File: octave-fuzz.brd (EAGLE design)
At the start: 77.1 x 81.3 mm, 56 parts, among them T1 2N5089, T2 2N5089, T3 2N5089, T4 2N5089, T5 2N5089

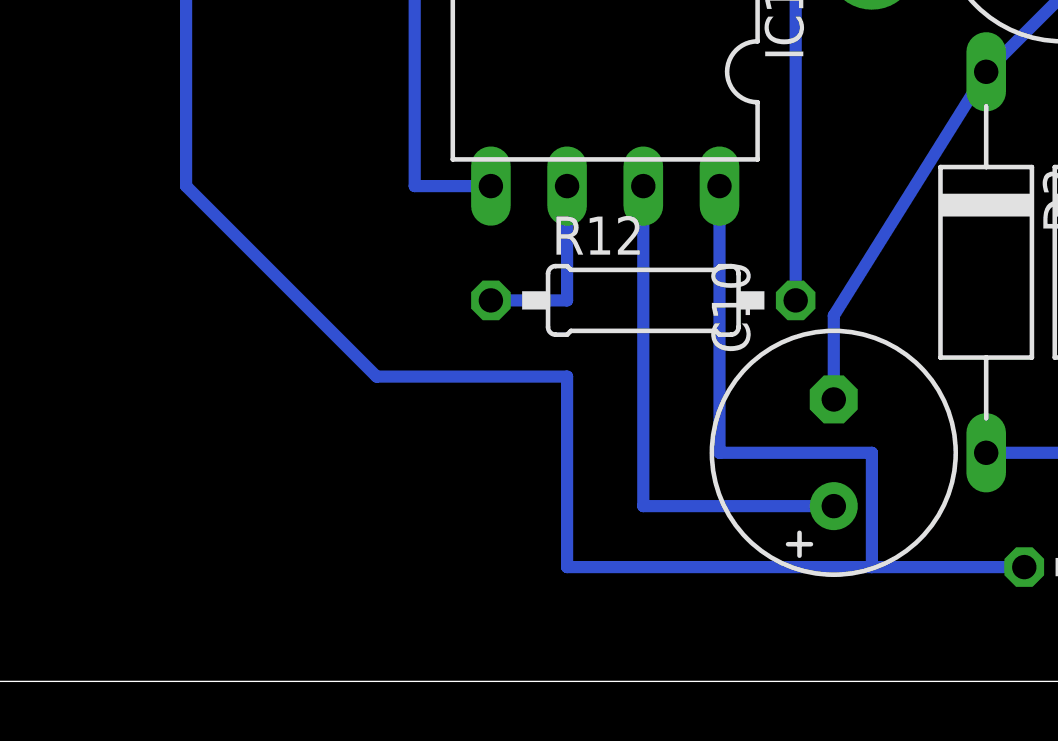
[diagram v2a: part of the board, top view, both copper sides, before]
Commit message: added a missing resistor and edited component values
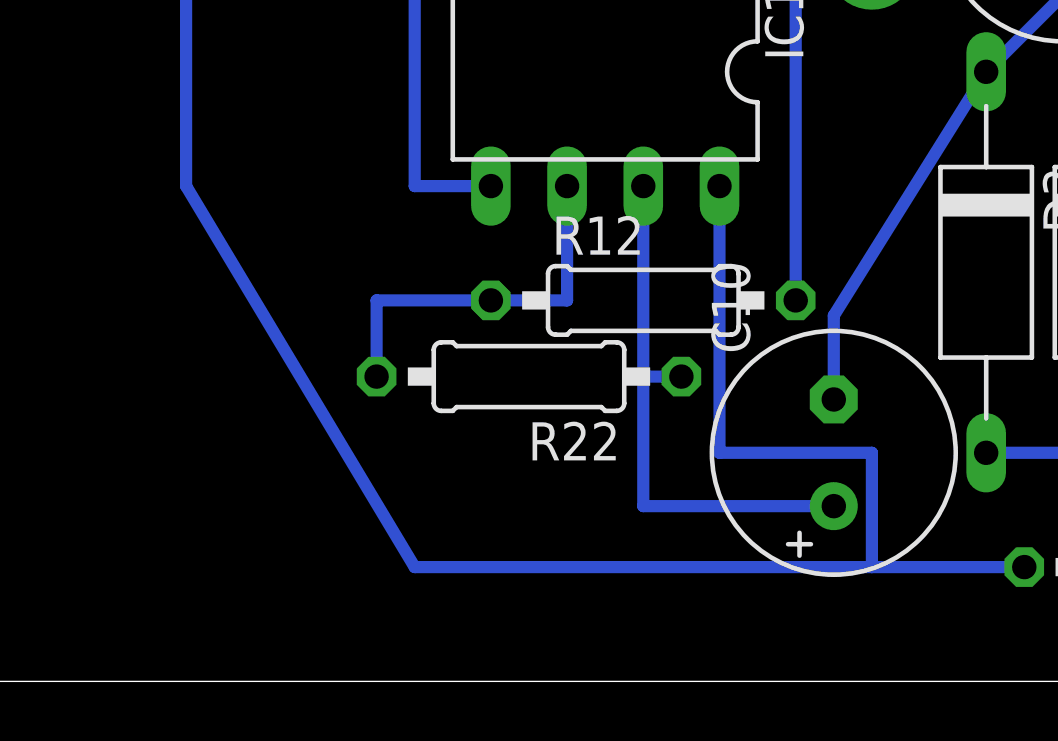
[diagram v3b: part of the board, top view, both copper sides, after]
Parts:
- added R22: 10k, resistor:0207/10
- C11: value (none) -> 10µF
- C12, C2: value (none) -> .47µF
- C13, C9: value (none) -> 100µF
- C3, C5, C6, C7: value (none) -> .1µF
- C4: value (none) -> 1µF
- C8: value (none) -> .01µF
- D1: value (none) -> 1N914
- IC1: value (none) -> NE5532
- R1, R21: value (none) -> 1M
- R10, R11, R14: value (none) -> 100k
- R12, R19, R20, R5, R6, R8, R9: value (none) -> 10k
- R13: value (none) -> 270
- R15, R17: value (none) -> 33k
- R16: value (none) -> 4.7k
- R18, R4: value (none) -> 220k
- R2: value (none) -> 2M
- R3: value (none) -> 3.3M
- R7: value (none) -> 47k
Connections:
- net N$21: now also R22.2
- net N$22: now also R22.1
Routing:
- net N$21: track 6.35 -> 12.7 mm
- net +9V: track 188.2 -> 186.4 mm
- net N$22: track 17.0 -> 18.3 mm
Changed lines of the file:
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@@
 <element name="C1" library="rcl" package="C050-025X075" value="" x="46.99" y="41.91" rot="R90"/>
 <element name="C10" library="rcl" package="E3,5-8" value="" x="50.8" y="6.35" rot="R90"/>
-<element name="C11" library="rcl" package="E3,5-8" value="" x="58.42" y="24.13"/>
-<element name="C12" library="rcl" package="C050-025X075" value="" x="71.12" y="20.32" rot="R90"/>
-<element name="C13" library="rcl" package="E3,5-8" value="" x="24.13" y="49.53" rot="R180"/>
-<element name="C2" library="rcl" package="C050-025X075" value="" x="40.64" y="66.04" rot="R180"/>
-<element name="C3" library="rcl" package="C050-025X075" value="" x="63.5" y="64.77" rot="R90"/>
-<element name="C4" library="rcl" package="E3,5-8" value="" x="39.37" y="72.39" rot="R90"/>
-<element name="C5" library="rcl" package="C050-025X075" value="" x="46.99" y="62.23"/>
-<element name="C6" library="rcl" package="C050-025X075" value="" x="57.15" y="62.23"/>
-<element name="C7" library="rcl" package="C050-025X075" value="" x="62.23" y="72.39"/>
-<element name="C8" library="rcl" package="C050-025X075" value="" x="43.18" y="34.29" rot="R270"/>
-<element name="C9" library="rcl" package="E3,5-8" value="" x="29.21" y="29.21" rot="R90"/>
-<element name="D1" library="diode" package="D-12.5" value="" x="39.37" y="55.88" rot="R90"/>
+<element name="C11" library="rcl" package="E3,5-8" value="10µF" x="58.42" y="24.13"/>
+<element name="C12" library="rcl" package="C050-025X075" value=".47µF" x="71.12" y="20.32" rot="R90"/>
+<element name="C13" library="rcl" package="E3,5-8" value="100µF" x="24.13" y="49.53" rot="R180"/>
+<element name="C2" library="rcl" package="C050-025X075" value=".47µF" x="40.64" y="66.04" rot="R180"/>
+<element name="C3" library="rcl" package="C050-025X075" value=".1µF" x="63.5" y="64.77" rot="R90"/>
+<element name="C4" library="rcl" package="E3,5-8" value="1µF" x="39.37" y="72.39" rot="R90"/>
+<element name="C5" library="rcl" package="C050-025X075" value=".1µF" x="46.99" y="62.23"/>
+<element name="C6" library="rcl" package="C050-025X075" value=".1µF" x="57.15" y="62.23"/>
+<element name="C7" library="rcl" package="C050-025X075" value=".1µF" x="62.23" y="72.39"/>
+<element name="C8" library="rcl" package="C050-025X075" value=".01µF" x="43.18" y="34.29" rot="R270"/>
+<element name="C9" library="rcl" package="E3,5-8" value="100µF" x="29.21" y="29.21" rot="R90"/>
+<element name="D1" library="diode" package="D-12.5" value="1N914" x="39.37" y="55.88" rot="R90"/>
 <element name="D2" library="diode" package="D-12.5" value="" x="59.69" y="12.7" rot="R270"/>
 <element name="D3" library="diode" package="D-12.5" value="" x="55.88" y="12.7" rot="R270"/>
@@
 <attribute name="TP_SIGNAL_NAME" value="" x="15.24" y="54.61" size="1.778" layer="27" display="off"/>
 </element>
-<element name="IC1" library="ic-package" package="DIL08" value="" x="43.18" y="19.05" rot="R180"/>
+<element name="IC1" library="ic-package" package="DIL08" value="NE5532" x="43.18" y="19.05" rot="R180"/>
 <element name="IN" library="testpad" package="P1-17Y" value="TPPAD1-17Y" x="43.18" y="40.64" rot="R180">
 <attribute name="TP_SIGNAL_NAME" value="" x="43.18" y="40.64" size="1.778" layer="27" rot="R180" display="off"/>
@@
 <attribute name="TP_SIGNAL_NAME" value="" x="67.31" y="44.45" size="1.778" layer="27" display="off"/>
 </element>
-<element name="R1" library="resistor" package="0207/10" value="" x="54.61" y="43.18" rot="R180"/>
-<element name="R10" library="resistor" package="0207/10" value="" x="49.53" y="54.61" rot="R270"/>
-<element name="R11" library="resistor" package="0207/10" value="" x="54.61" y="54.61" rot="R270"/>
-<element name="R12" library="resistor" package="0207/10" value="" x="44.45" y="11.43"/>
-<element name="R13" library="resistor" package="0207/10" value="" x="39.37" y="26.67"/>
-<element name="R14" library="resistor" package="0207/10" value="" x="62.23" y="2.54" rot="R180"/>
-<element name="R15" library="resistor" package="0207/10" value="" x="59.69" y="34.29" rot="R270"/>
-<element name="R16" library="resistor" package="0207/10" value="" x="35.56" y="38.1" rot="R270"/>
-<element name="R17" library="resistor" package="0207/10" value="" x="55.88" y="34.29" rot="R270"/>
-<element name="R18" library="resistor" package="0207/10" value="" x="39.37" y="38.1" rot="R90"/>
-<element name="R19" library="resistor" package="0207/10" value="" x="24.13" y="40.64" rot="R180"/>
-<element name="R2" library="resistor" package="0207/10" value="" x="17.78" y="69.85" rot="R270"/>
-<element name="R20" library="resistor" package="0207/10" value="" x="30.48" y="46.99" rot="R270"/>
-<element name="R21" library="pot" package="CA9V" value="" x="72.39" y="69.85" rot="R270"/>
-<element name="R3" library="resistor" package="0207/10" value="" x="20.32" y="64.77" rot="R90"/>
-<element name="R4" library="resistor" package="0207/10" value="" x="26.67" y="69.85" rot="R270"/>
-<element name="R5" library="resistor" package="0207/10" value="" x="55.88" y="46.99" rot="R180"/>
-<element name="R6" library="resistor" package="0207/10" value="" x="45.72" y="72.39" rot="R90"/>
-<element name="R7" library="resistor" package="0207/10" value="" x="33.02" y="72.39" rot="R90"/>
-<element name="R8" library="resistor" package="0207/10" value="" x="44.45" y="54.61" rot="R270"/>
-<element name="R9" library="resistor" package="0207/10" value="" x="59.69" y="54.61" rot="R270"/>
+<element name="R1" library="resistor" package="0207/10" value="1M" x="54.61" y="43.18" rot="R180"/>
+<element name="R10" library="resistor" package="0207/10" value="100k" x="49.53" y="54.61" rot="R270"/>
+<element name="R11" library="resistor" package="0207/10" value="100k" x="54.61" y="54.61" rot="R270"/>
+<element name="R12" library="resistor" package="0207/10" value="10k" x="44.45" y="11.43"/>
+<element name="R13" library="resistor" package="0207/10" value="270" x="39.37" y="26.67"/>
+<element name="R14" library="resistor" package="0207/10" value="100k" x="62.23" y="2.54" rot="R180"/>
+<element name="R15" library="resistor" package="0207/10" value="33k" x="59.69" y="34.29" rot="R270"/>
+<element name="R16" library="resistor" package="0207/10" value="4.7k" x="35.56" y="38.1" rot="R270"/>
+<element name="R17" library="resistor" package="0207/10" value="33k" x="55.88" y="34.29" rot="R270"/>
+<element name="R18" library="resistor" package="0207/10" value="220k" x="39.37" y="38.1" rot="R90"/>
+<element name="R19" library="resistor" package="0207/10" value="10k" x="24.13" y="40.64" rot="R180"/>
+<element name="R2" library="resistor" package="0207/10" value="2M" x="17.78" y="69.85" rot="R270"/>
+<element name="R20" library="resistor" package="0207/10" value="10k" x="30.48" y="46.99" rot="R270"/>
+<element name="R21" library="pot" package="CA9V" value="1M" x="72.39" y="69.85" rot="R270"/>
+<element name="R3" library="resistor" package="0207/10" value="3.3M" x="20.32" y="64.77" rot="R90"/>
+<element name="R4" library="resistor" package="0207/10" value="220k" x="26.67" y="69.85" rot="R270"/>
+<element name="R5" library="resistor" package="0207/10" value="10k" x="55.88" y="46.99" rot="R180"/>
+<element name="R6" library="resistor" package="0207/10" value="10k" x="45.72" y="72.39" rot="R90"/>
+<element name="R7" library="resistor" package="0207/10" value="47k" x="33.02" y="72.39" rot="R90"/>
+<element name="R8" library="resistor" package="0207/10" value="10k" x="44.45" y="54.61" rot="R270"/>
+<element name="R9" library="resistor" package="0207/10" value="10k" x="59.69" y="54.61" rot="R270"/>
 <element name="T1" library="transistor" package="TO92" value="2N5089" x="33.02" y="55.88" rot="R180"/>
 <element name="T2" library="transistor" package="TO92" value="2N5089" x="64.77" y="58.42" rot="R180"/>
@@
 <element name="T4" library="transistor" package="TO92" value="2N5089" x="49.53" y="69.85" rot="R270"/>
 <element name="T5" library="transistor" package="TO92" value="2N5089" x="55.88" y="68.58" rot="R270"/>
+<element name="R22" library="resistor" package="0207/10" value="10k" x="40.64" y="8.89" rot="R180"/>
 </elements>
 <signals>
@@
 <wire x1="20.32" y1="69.85" x2="24.13" y2="66.04" width="0.4064" layer="16"/>
 <wire x1="24.13" y1="66.04" x2="24.13" y2="64.77" width="0.4064" layer="16"/>
-<wire x1="29.21" y1="15.24" x2="35.56" y2="8.89" width="0.4064" layer="16"/>
-<wire x1="35.56" y1="8.89" x2="41.91" y2="8.89" width="0.4064" layer="16"/>
-<wire x1="41.91" y1="8.89" x2="41.91" y2="2.54" width="0.4064" layer="16"/>
-<wire x1="41.91" y1="2.54" x2="52.07" y2="2.54" width="0.4064" layer="16"/>
+<wire x1="29.21" y1="15.24" x2="36.83" y2="2.54" width="0.4064" layer="16"/>
+<wire x1="36.83" y1="2.54" x2="52.07" y2="2.54" width="0.4064" layer="16"/>
 <wire x1="52.07" y1="2.54" x2="52.07" y2="6.35" width="0.4064" layer="16"/>
 <wire x1="52.07" y1="6.35" x2="46.99" y2="6.35" width="0.4064" layer="16"/>
@@
 <wire x1="39.37" y1="11.43" x2="41.91" y2="11.43" width="0.4064" layer="16"/>
 <wire x1="41.91" y1="11.43" x2="41.91" y2="15.24" width="0.4064" layer="16"/>
+<contactref element="R22" pad="2"/>
+<wire x1="35.56" y1="8.89" x2="35.56" y2="11.43" width="0.4064" layer="16"/>
+<wire x1="35.56" y1="11.43" x2="39.37" y2="11.43" width="0.4064" layer="16"/>
 </signal>
 <signal name="N$18">
@@
 <contactref element="C10" pad="+"/>
 <wire x1="50.8" y1="4.572" x2="44.45" y2="4.572" width="0.4064" layer="16"/>
-<wire x1="44.45" y1="4.572" x2="44.45" y2="15.24" width="0.4064" layer="16"/>
+<wire x1="44.45" y1="4.572" x2="44.45" y2="8.89" width="0.4064" layer="16"/>
+<contactref element="R22" pad="1"/>
+<wire x1="44.45" y1="8.89" x2="44.45" y2="15.24" width="0.4064" layer="16"/>
+<wire x1="45.72" y1="8.89" x2="44.45" y2="8.89" width="0.4064" layer="16"/>
 </signal>
 <signal name="N$23">
